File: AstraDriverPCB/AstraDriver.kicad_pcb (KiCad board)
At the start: 2 copper layers, 10 x 12 mm, 2 parts

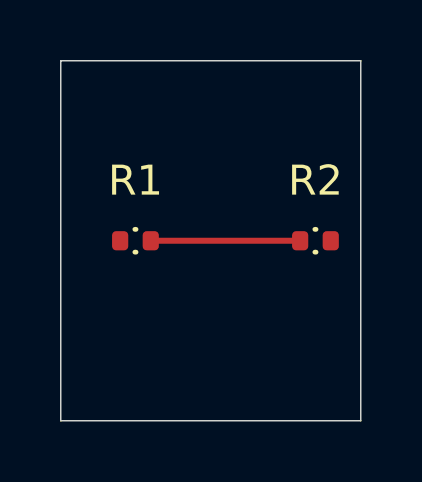
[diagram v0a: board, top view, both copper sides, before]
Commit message: Update board dimensions and center
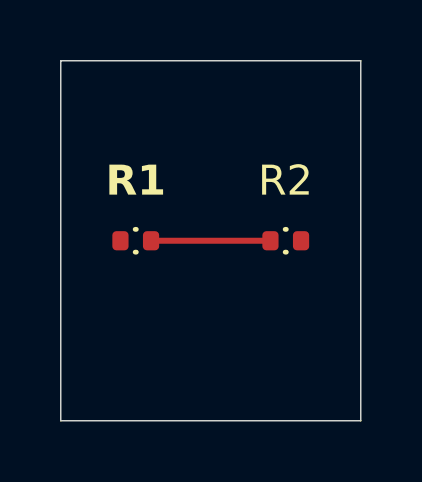
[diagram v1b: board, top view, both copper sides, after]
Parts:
- moved R2 0.99 mm to (147.5, 86.0)
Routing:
- net Net-(R1-Pad2): track 4.98 -> 3.98 mm
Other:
- copper layers 2 -> 4
- rule pad_to_mask_clearance: 0 -> 0.04
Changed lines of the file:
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@@
 	(generator_version "8.0")
 	(general
-		(thickness 1.6)
+		(thickness 1.6062)
 		(legacy_teardrops no)
 	)
 	(paper "A4")
 	(layers
-		(0 "F.Cu" signal)
-		(31 "B.Cu" signal)
+		(0 "F.Cu" mixed)
+		(1 "In1.Cu" power)
+		(2 "In2.Cu" power)
+		(31 "B.Cu" mixed)
 		(32 "B.Adhes" user "B.Adhesive")
 		(33 "F.Adhes" user "F.Adhesive")
@@
 		(49 "F.Fab" user)
 		(50 "User.1" user)
-		(51 "User.2" user)
+		(51 "User.2" user "Board.Alignment")
 		(52 "User.3" user)
 		(53 "User.4" user)
-		(54 "User.5" user)
+		(54 "User.5" user "Board.Center")
 		(55 "User.6" user)
 		(56 "User.7" user)
-		(57 "User.8" user)
-		(58 "User.9" user)
+		(57 "User.8" user "Board.Dimensions")
+		(58 "User.9" user "Board.Title")
 	)
 	(setup
-		(pad_to_mask_clearance 0)
+		(stackup
+			(layer "F.SilkS"
+				(type "Top Silk Screen")
+				(color "White")
+			)
+			(layer "F.Paste"
+				(type "Top Solder Paste")
+			)
+			(layer "F.Mask"
+				(type "Top Solder Mask")
+				(color "#0000002B")
+				(thickness 0.01)
+			)
+			(layer "F.Cu"
+				(type "copper")
+				(thickness 0.035)
+			)
+			(layer "dielectric 1"
+				(type "prepreg")
+				(color "FR4 natural")
+				(thickness 0.2104)
+				(material "FR4")
+				(epsilon_r 4.4)
+				(loss_tangent 0.02)
+			)
+			(layer "In1.Cu"
+				(type "copper")
+				(thickness 0.0152)
+			)
+			(layer "dielectric 2"
+				(type "core")
+				(color "FR4 natural")
+				(thickness 1.065)
+				(material "FR4")
+				(epsilon_r 4.6)
+				(loss_tangent 0.02)
+			)
+			(layer "In2.Cu"
+				(type "copper")
+				(thickness 0.0152)
+			)
+			(layer "dielectric 3"
+				(type "prepreg")
+				(color "FR4 natural")
+				(thickness 0.2104)
+				(material "FR4")
+				(epsilon_r 4.4)
+				(loss_tangent 0.02)
+			)
+			(layer "B.Cu"
+				(type "copper")
+				(thickness 0.035)
+			)
+			(layer "B.Mask"
+				(type "Bottom Solder Mask")
+				(color "#0000002B")
+				(thickness 0.01)
+			)
+			(layer "B.Paste"
+				(type "Bottom Solder Paste")
+			)
+			(layer "B.SilkS"
+				(type "Bottom Silk Screen")
+				(color "White")
+			)
+			(copper_finish "ENIG")
+			(dielectric_constraints yes)
+		)
+		(pad_to_mask_clearance 0.04)
+		(solder_mask_min_width 0.102)
 		(allow_soldermask_bridges_in_footprints no)
 		(pcbplotparams
@@
 	(footprint "LiveAstra:R_0402_1005Metric"
 		(layer "F.Cu")
-		(at 148.49 86)
+		(at 147.5 86)
 		(descr "Resistor SMD 0402 (1005 Metric), square (rectangular) end terminal, IPC_7351 nominal, (Body size source: IPC-SM-782 page 72, https://www.pcb-3d.com/wordpress/wp-content/uploads/ipc-sm-782a_amendment_1_and_2.pdf), generated with kicad-footprint-generator")
 		(tags "resistor")
 		(property "Reference" "R2"
-			(at 0 -2 0)
+			(at -0.01 -2 0)
 			(layer "F.SilkS")
 			(effects
 				(font
 					(size 1 1)
-					(thickness 0.15)
+					(thickness 0.2)
 				)
 			)
@@
 	(footprint "LiveAstra:R_0402_1005Metric"
 		(layer "F.Cu")
-		(at 142.49 86)
+		(at 142.5 86)
 		(descr "Resistor SMD 0402 (1005 Metric), square (rectangular) end terminal, IPC_7351 nominal, (Body size source: IPC-SM-782 page 72, https://www.pcb-3d.com/wordpress/wp-content/uploads/ipc-sm-782a_amendment_1_and_2.pdf), generated with kicad-footprint-generator")
 		(tags "resistor")
 		(property "Reference" "R1"
-			(at 0 -2 360)
+			(at 0 -2 0)
 			(layer "F.SilkS")
 			(effects
 				(font
 					(size 1 1)
-					(thickness 0.15)
+					(thickness 0.2)
+					(bold yes)
 				)
 			)
@@
 		(layer "Edge.Cuts")
 	)
+	(gr_rect
+		(start 139 80)
+		(end 151 92)
+		(stroke
+			(width 0.15)
+			(type default)
+		)
+		(fill none)
+		(layer "User.5")
+	)
+	(gr_rect
+		(start 139 80)
+		(end 151 92)
+		(stroke
+			(width 0.15)
+			(type default)
+		)
+		(fill none)
+		(layer "User.8")
+	)
 	(segment
-		(start 147.98 86)
-		(end 143 86)
+		(start 146.99 86)
+		(end 143.01 86)
 		(width 0.2)
 		(layer "F.Cu")

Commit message: Progress
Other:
- board text added: "${TITLE}"
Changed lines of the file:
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@@
 		)
 		(property "Value" "10"
-			(at 0 2 360)
+			(at 0 2 0)
 			(layer "F.Fab")
 			(effects
@@
 		)
 		(fp_text user "${REFERENCE}"
-			(at 0 1 360)
+			(at 0 1 0)
 			(layer "F.Fab")
 			(effects
@@
 		)
 		(fill none)
-		(layer "User.5")
+		(layer "User.2")
 	)
 	(gr_rect
@@
 		)
 		(fill none)
+		(layer "User.5")
+	)
+	(gr_rect
+		(start 139 80)
+		(end 151 92)
+		(stroke
+			(width 0.15)
+			(type default)
+		)
+		(fill none)
 		(layer "User.8")
 	)
+	(gr_text "${TITLE}"
+		(at 145 77.5 0)
+		(layer "User.9")
+		(effects
+			(font
+				(face "ING Me Headline")
+				(size 4 4)
+				(thickness 0.15)
+			)
+		)
+		(render_cache "" 0)
+	)
 	(segment

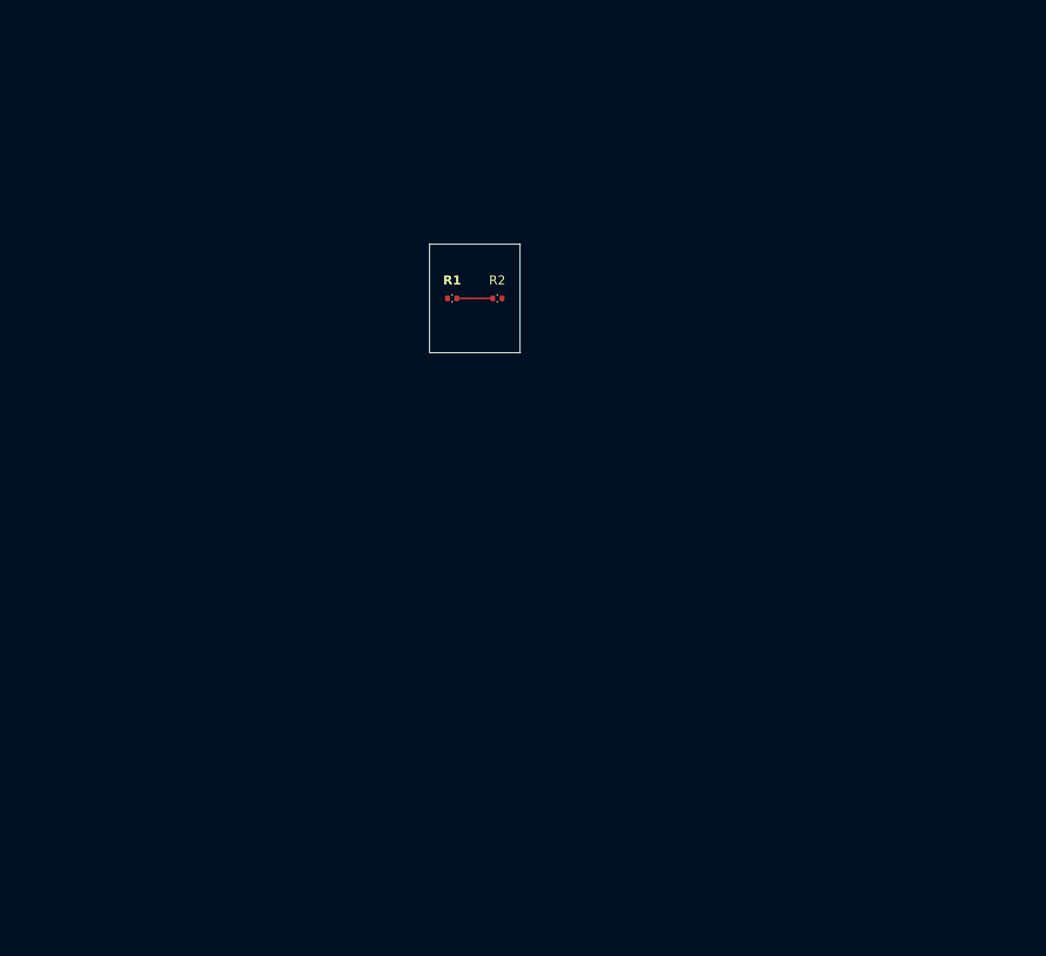
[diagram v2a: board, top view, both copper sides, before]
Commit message: Added all schematic components
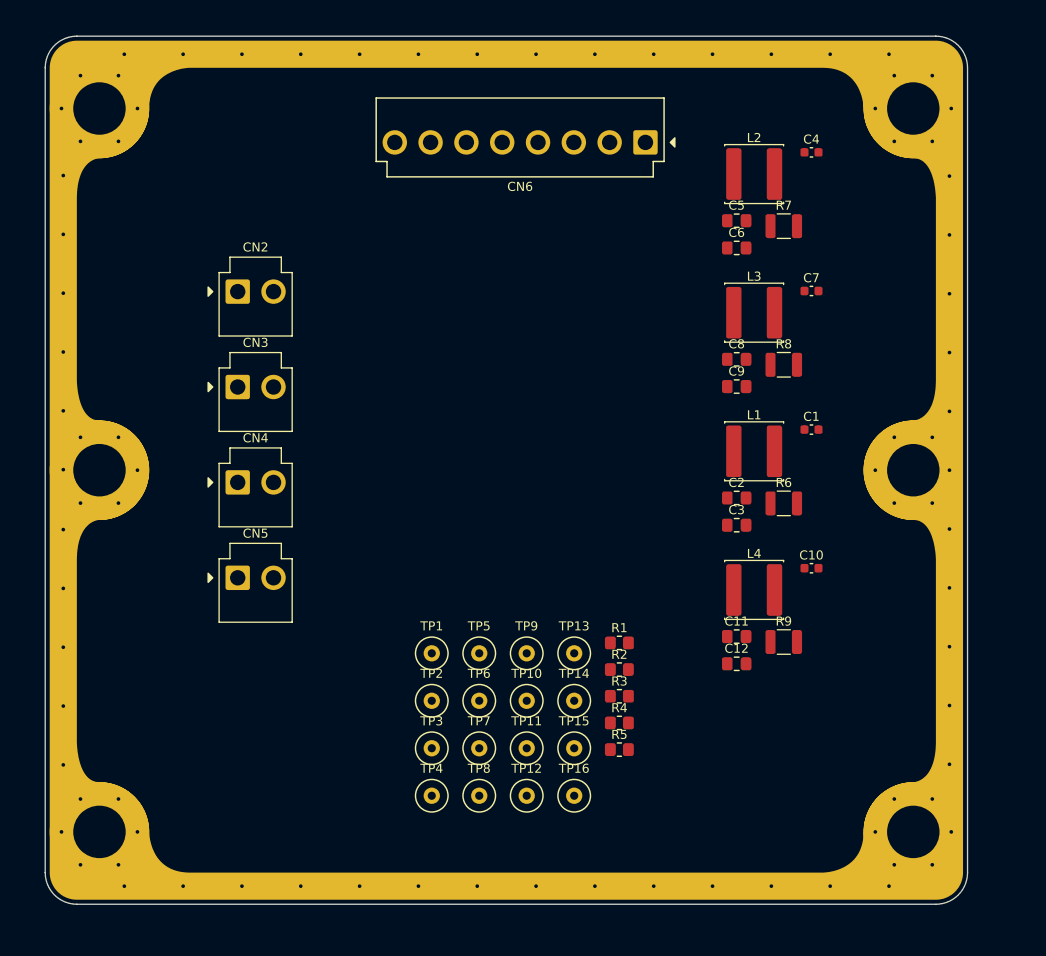
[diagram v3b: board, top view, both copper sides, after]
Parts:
- added C1: 22u, LiveAstra:C_0603_1608Metric, F.Cu at (182.2, 100.5)
- added C10: 22u, LiveAstra:C_0603_1608Metric, F.Cu at (182.2, 115.8)
- added C11: 1u, LiveAstra:C_0805_2012Metric_Pad1.18x1.45mm_HandSolder, F.Cu at (174.0, 123.4)
- added C12: 1u, LiveAstra:C_0805_2012Metric_Pad1.18x1.45mm_HandSolder, F.Cu at (174.0, 126.4)
- added C2: 1u, LiveAstra:C_0805_2012Metric_Pad1.18x1.45mm_HandSolder, F.Cu at (174.0, 108.1)
- added C3: 1u, LiveAstra:C_0805_2012Metric_Pad1.18x1.45mm_HandSolder, F.Cu at (174.0, 111.1)
- added C4: 22u, LiveAstra:C_0603_1608Metric, F.Cu at (182.2, 69.8)
- added C5: 1u, LiveAstra:C_0805_2012Metric_Pad1.18x1.45mm_HandSolder, F.Cu at (174.0, 77.4)
- added C6: 1u, LiveAstra:C_0805_2012Metric_Pad1.18x1.45mm_HandSolder, F.Cu at (174.0, 80.4)
- added C7: 22u, LiveAstra:C_0603_1608Metric, F.Cu at (182.2, 85.2)
- added C8: 1u, LiveAstra:C_0805_2012Metric_Pad1.18x1.45mm_HandSolder, F.Cu at (174.0, 92.7)
- added C9: 1u, LiveAstra:C_0805_2012Metric_Pad1.18x1.45mm_HandSolder, F.Cu at (174.0, 95.8)
- added CN2: JST VH 2 PIN, LiveAstra:JST_VH_B2P-VH-B_1x02_P3.96mm_Vertical, F.Cu at (120.8, 85.2)
- added CN3: JST VH 2 PIN, LiveAstra:JST_VH_B2P-VH-B_1x02_P3.96mm_Vertical, F.Cu at (120.8, 95.8)
- added CN4: JST VH 2 PIN, LiveAstra:JST_VH_B2P-VH-B_1x02_P3.96mm_Vertical, F.Cu at (120.8, 106.3)
- added CN5: JST VH 2 PIN, LiveAstra:JST_VH_B2P-VH-B_1x02_P3.96mm_Vertical, F.Cu at (120.8, 116.9)
- added CN6: JST VH 8 PIN, LiveAstra:JST_VH_B8P-VH-B_1x08_P3.96mm_Vertical, F.Cu at (150.0, 68.8)
- added L1: 4u7H, LiveAstra:L_Sunlord_SWPA6045S, F.Cu at (175.9, 102.9)
- added L2: 4u7H, LiveAstra:L_Sunlord_SWPA6045S, F.Cu at (175.9, 72.2)
- added L3: 4u7H, LiveAstra:L_Sunlord_SWPA6045S, F.Cu at (175.9, 87.6)
- added L4: 4u7H, LiveAstra:L_Sunlord_SWPA6045S, F.Cu at (175.9, 118.2)
- added R3: 0, LiveAstra:R_0805_2012Metric_Pad1.20x1.40mm_HandSolder, F.Cu at (161.0, 130.0)
- added R4: 0, LiveAstra:R_0805_2012Metric_Pad1.20x1.40mm_HandSolder, F.Cu at (161.0, 132.9)
- added R5: 0, LiveAstra:R_0805_2012Metric_Pad1.20x1.40mm_HandSolder, F.Cu at (161.0, 135.9)
- added R6: 40m, LiveAstra:R_1210_3225Metric, F.Cu at (179.2, 108.7)
- added R7: 40m, LiveAstra:R_1210_3225Metric, F.Cu at (179.2, 78.0)
- added R8: 40m, LiveAstra:R_1210_3225Metric, F.Cu at (179.2, 93.3)
- added R9: 47m, LiveAstra:R_1210_3225Metric, F.Cu at (179.2, 124.0)
- added RING1: ~, LiveAstra:AstraControl_Ground_Ring, F.Cu at (148.5, 105.0)
- added TP1: TestPoint_Thimble, LiveAstra:TestPoint_Loop_D3.50mm_Drill0.9mm_Beaded, F.Cu at (140.2, 125.2)
- added TP10: TestPoint_Thimble, LiveAstra:TestPoint_Loop_D3.50mm_Drill0.9mm_Beaded, F.Cu at (150.8, 130.5)
- added TP11: TestPoint_Thimble, LiveAstra:TestPoint_Loop_D3.50mm_Drill0.9mm_Beaded, F.Cu at (150.8, 135.8)
- added TP12: TestPoint_Thimble, LiveAstra:TestPoint_Loop_D3.50mm_Drill0.9mm_Beaded, F.Cu at (150.8, 141.0)
- added TP13: TestPoint_Thimble, LiveAstra:TestPoint_Loop_D3.50mm_Drill0.9mm_Beaded, F.Cu at (156.0, 125.2)
- added TP14: TestPoint_Thimble, LiveAstra:TestPoint_Loop_D3.50mm_Drill0.9mm_Beaded, F.Cu at (156.0, 130.5)
- added TP15: TestPoint_Thimble, LiveAstra:TestPoint_Loop_D3.50mm_Drill0.9mm_Beaded, F.Cu at (156.0, 135.8)
- added TP16: TestPoint_Thimble, LiveAstra:TestPoint_Loop_D3.50mm_Drill0.9mm_Beaded, F.Cu at (156.0, 141.0)
- added TP2: TestPoint_Thimble, LiveAstra:TestPoint_Loop_D3.50mm_Drill0.9mm_Beaded, F.Cu at (140.2, 130.5)
- added TP3: TestPoint_Thimble, LiveAstra:TestPoint_Loop_D3.50mm_Drill0.9mm_Beaded, F.Cu at (140.2, 135.8)
- added TP4: TestPoint_Thimble, LiveAstra:TestPoint_Loop_D3.50mm_Drill0.9mm_Beaded, F.Cu at (140.2, 141.0)
- added TP5: TestPoint_Thimble, LiveAstra:TestPoint_Loop_D3.50mm_Drill0.9mm_Beaded, F.Cu at (145.5, 125.2)
- added TP6: TestPoint_Thimble, LiveAstra:TestPoint_Loop_D3.50mm_Drill0.9mm_Beaded, F.Cu at (145.5, 130.5)
- added TP7: TestPoint_Thimble, LiveAstra:TestPoint_Loop_D3.50mm_Drill0.9mm_Beaded, F.Cu at (145.5, 135.8)
- added TP8: TestPoint_Thimble, LiveAstra:TestPoint_Loop_D3.50mm_Drill0.9mm_Beaded, F.Cu at (145.5, 141.0)
- added TP9: TestPoint_Thimble, LiveAstra:TestPoint_Loop_D3.50mm_Drill0.9mm_Beaded, F.Cu at (150.8, 125.2)
- R1, R2: value 10 -> 0; footprint LiveAstra:R_0402_1005Metric -> LiveAstra:R_0805_2012Metric_Pad1.20x1.40mm_HandSolder
- moved R2 43.2 mm to (161.0, 127.0)
- moved R1 42.4 mm to (161.0, 124.1)
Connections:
- R1 pad 1: GND -> /Block Diagram/PWM_CH4
- R1 pad 2: Net-(R1-Pad2) -> /Block Diagram/Channel 4 2A/DIM
- R2 pad 1: Net-(R1-Pad2) -> /Block Diagram/PWM_CH3
- R2 pad 2: unconnected-(R2-Pad2) -> /Block Diagram/Channel 3 2.5A/DIM
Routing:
- net Net-(R1-Pad2): track 3.98 -> 0.00 mm
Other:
- board size 10 x 12 mm -> 102 x 96 mm

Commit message: progress
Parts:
- removed C10: 22u, LiveAstra:C_0603_1608Metric
- removed C11, C12: 1u, LiveAstra:C_0805_2012Metric_Pad1.18x1.45mm_HandSolder
- added C13: 1u, LiveAstra:C_0805_2012Metric_Pad1.18x1.45mm_HandSolder, F.Cu at (178.8, 101.2)
- added C14: 1u, LiveAstra:C_0805_2012Metric_Pad1.18x1.45mm_HandSolder, F.Cu at (157.7, 114.2)
- added C15: 1u, LiveAstra:C_0805_2012Metric_Pad1.18x1.45mm_HandSolder, F.Cu at (141.2, 115.5)
- added U1: LED2001PHR, LiveAstra:U_LED2001PHR_HSOP8, F.Cu at (177.5, 108.6)
- added U2: LED2001PHR, LiveAstra:U_LED2001PHR_HSOP8, F.Cu at (157.3, 101.6)
- added U3: LED2001PHR, LiveAstra:U_LED2001PHR_HSOP8, F.Cu at (140.7, 106.7)
- added U4: LED2001PHR, LiveAstra:U_LED2001PHR_HSOP8, F.Cu at (117.8, 116.6)
- C1, C4, C7: footprint LiveAstra:C_0603_1608Metric -> LiveAstra:C_0805_2012Metric_Pad1.18x1.45mm_HandSolder
- C9: value 1u -> 22u
- moved C6 71.9 mm to (114.8, 121.3)
- moved C8 67.0 mm to (114.8, 124.3)
- moved CN5 59.9 mm to (175.5, 141.2), turned to 180 degrees
- moved TP8 58.5 mm to (162.2, 85.0)
- moved TP4 57.3 mm to (142.8, 83.8)
- moved R5 56.9 mm to (162.2, 79.0), turned to -90 degrees
- moved CN2 56.0 mm to (121.5, 141.2), turned to 180 degrees
- moved L4 54.5 mm to (121.8, 124.0)
- moved R4 54.0 mm to (157.8, 79.0), turned to -90 degrees
- moved R9 53.7 mm to (125.7, 118.5)
- moved C7 53.4 mm to (137.0, 113.5)
- moved C9 53.3 mm to (124.5, 115.5)
- moved TP7 52.9 mm to (157.8, 84.2)
- moved TP3 52.3 mm to (137.2, 83.5)
- moved R3 51.9 mm to (153.0, 78.8), turned to -90 degrees
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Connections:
- net /Block Diagram/Channel 1 2.5A/DIM renamed /Block Diagram/DIM_1
- net /Block Diagram/Channel 1 2.5A/LED- renamed /Block Diagram/CH1_LED-
- net /Block Diagram/Channel 2 2.5A/DIM renamed /Block Diagram/DIM_2
- net /Block Diagram/Channel 3 2.5A/DIM renamed /Block Diagram/DIM_3
- net /Block Diagram/Channel 4 2A/DIM renamed /Block Diagram/DIM_4
- net Net-(R5-Pad2) renamed /Block Diagram/RSRV
- C3 pad 2: /Block Diagram/Channel 1 2.5A/LED+ -> +5V
- C6 pad 2: /Block Diagram/Channel 2 2.5A/LED+ -> /Block Diagram/CH4_LED+
- C9 pad 2: /Block Diagram/Channel 3 2.5A/LED+ -> +5V
- CN2 pad 1: /Block Diagram/Channel 4 2A/LED+ -> /Block Diagram/CH4_LED+
- CN2 pad 2: /Block Diagram/Channel 4 2A/LED- -> /Block Diagram/CH4_LED+
- CN3 pad 1: /Block Diagram/Channel 3 2.5A/LED+ -> /Block Diagram/CH3_LED+
- CN3 pad 2: /Block Diagram/Channel 3 2.5A/LED- -> /Block Diagram/CH3_LED+
- CN4 pad 1: /Block Diagram/Channel 2 2.5A/LED+ -> /Block Diagram/CH2_LED+
- CN4 pad 2: /Block Diagram/Channel 2 2.5A/LED- -> /Block Diagram/CH2_LED+
- CN5 pad 1: /Block Diagram/Channel 1 2.5A/LED+ -> /Block Diagram/CH1_LED+
- CN6 pad 1: /Block Diagram/RESERVED -> +5V
- CN6 pad 2: /Block Diagram/PWM_CH1 -> +3V3
- CN6 pad 3: /Block Diagram/PWM_CH2 -> GND
- CN6 pad 4: /Block Diagram/PWM_CH3 -> /Block Diagram/PWM_CH4
- CN6 pad 5: /Block Diagram/PWM_CH4 -> /Block Diagram/PWM_CH3
- CN6 pad 6: GND -> /Block Diagram/PWM_CH2
- CN6 pad 7: +3V3 -> /Block Diagram/PWM_CH1
- CN6 pad 8: +5V -> /Block Diagram/RESERVED
- L1 pad 1: Net-(U1-SW) -> /Block Diagram/Channel 1 2.5A/SW_OUT
- L1 pad 2: /Block Diagram/Channel 1 2.5A/LED+ -> /Block Diagram/CH1_LED+
- L2 pad 1: Net-(U2-SW) -> /Block Diagram/Channel 2 2.5A/SW_OUT
- L2 pad 2: /Block Diagram/Channel 2 2.5A/LED+ -> /Block Diagram/CH2_LED+
- L3 pad 1: Net-(U3-SW) -> /Block Diagram/Channel 3 2.5A/SW_OUT
- L3 pad 2: /Block Diagram/Channel 3 2.5A/LED+ -> /Block Diagram/CH3_LED+
- L4 pad 1: Net-(U4-SW) -> /Block Diagram/Channel 4 2A/SW_OUT
- L4 pad 2: /Block Diagram/Channel 4 2A/LED+ -> /Block Diagram/CH4_LED+
- R7 pad 2: /Block Diagram/Channel 2 2.5A/LED- -> /Block Diagram/CH2_LED+
- R8 pad 2: /Block Diagram/Channel 3 2.5A/LED- -> /Block Diagram/CH3_LED+
- R9 pad 2: /Block Diagram/Channel 4 2A/LED- -> /Block Diagram/CH4_LED+
- TP10 pad 1: /Block Diagram/Channel 4 2A/LED- -> /Block Diagram/CH4_LED+
- TP11 pad 1: /Block Diagram/Channel 3 2.5A/LED+ -> /Block Diagram/CH3_LED+
- TP12 pad 1: /Block Diagram/Channel 3 2.5A/LED- -> /Block Diagram/CH3_LED+
- TP13 pad 1: /Block Diagram/Channel 2 2.5A/LED+ -> /Block Diagram/CH2_LED+
- TP14 pad 1: /Block Diagram/Channel 2 2.5A/LED- -> /Block Diagram/CH2_LED+
- TP15 pad 1: /Block Diagram/Channel 1 2.5A/LED+ -> /Block Diagram/CH1_LED+
- TP9 pad 1: /Block Diagram/Channel 4 2A/LED+ -> /Block Diagram/CH4_LED+
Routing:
- net GND: vias 0 -> 4
- net /Block Diagram/Channel 1 2.5A/SW_OUT: vias 0 -> 5
- added copper zone on F.Cu, net /Block Diagram/Channel 1 2.5A/SW_OUT

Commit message: Finished layout
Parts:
- added R10: 0, LiveAstra:R_0805_2012Metric_Pad1.20x1.40mm_HandSolder, F.Cu at (133.2, 78.8)
- moved L4 22.8 mm to (115.7, 102.0), turned to 180 degrees
- moved L3 18.9 mm to (133.7, 102.0), turned to 180 degrees
- moved C3 18.0 mm to (157.4, 113.2)
- moved C6 14.4 mm to (116.2, 107.0), turned to 180 degrees
- moved L1 14.1 mm to (169.7, 102.0), turned to 180 degrees
- moved C9 13.5 mm to (123.8, 102.0)
- moved TP8 13.3 mm to (175.5, 85.5)
- moved R8 12.9 mm to (144.5, 114.0), turned to 180 degrees
- moved C8 12.9 mm to (121.4, 113.2)
- moved C7 12.4 mm to (141.8, 102.0)
- moved C15 11.0 mm to (134.2, 107.0), turned to 180 degrees
- moved U4 10.5 mm to (124.4, 108.5), turned to 90 degrees
- moved C13 10.3 mm to (170.2, 107.0), turned to 180 degrees
- moved TP7 10.1 mm to (167.8, 85.5)
- moved L2 9.42 mm to (151.7, 102.0), turned to 180 degrees
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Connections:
- CN2 pad 1: /Block Diagram/CH4_LED+ -> /Block Diagram/CH4_LED-
- CN3 pad 1: /Block Diagram/CH3_LED+ -> /Block Diagram/CH3_LED-
- CN4 pad 1: /Block Diagram/CH2_LED+ -> /Block Diagram/CH2_LED-
- CN5 pad 1: /Block Diagram/CH1_LED+ -> /Block Diagram/CH1_LED-
- CN5 pad 2: /Block Diagram/CH1_LED- -> /Block Diagram/CH1_LED+
- CN6 pad 2: +3V3 -> /Block Diagram/3V3_R
- R7 pad 2: /Block Diagram/CH2_LED+ -> /Block Diagram/CH2_LED-
- R8 pad 2: /Block Diagram/CH3_LED+ -> /Block Diagram/CH3_LED-
- R9 pad 2: /Block Diagram/CH4_LED+ -> /Block Diagram/CH4_LED-
- TP11 pad 1: /Block Diagram/CH3_LED+ -> /Block Diagram/CH3_LED-
- TP13 pad 1: /Block Diagram/CH2_LED+ -> /Block Diagram/CH2_LED-
- TP15 pad 1: /Block Diagram/CH1_LED+ -> /Block Diagram/CH1_LED-
- TP16 pad 1: /Block Diagram/CH1_LED- -> /Block Diagram/CH1_LED+
- TP9 pad 1: /Block Diagram/CH4_LED+ -> /Block Diagram/CH4_LED-
- U2 pad 3: /Block Diagram/CH2_LED+ -> /Block Diagram/CH2_LED-
- U3 pad 3: /Block Diagram/CH3_LED+ -> /Block Diagram/CH3_LED-
- U4 pad 3: /Block Diagram/CH4_LED+ -> /Block Diagram/CH4_LED-
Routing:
- net /Block Diagram/DIM_1: track 0.00 -> 52.7 mm, vias 0 -> 2
- net /Block Diagram/DIM_4: track 0.00 -> 50.6 mm, vias 0 -> 2
- net /Block Diagram/DIM_2: track 0.00 -> 43.7 mm, vias 0 -> 2
- net /Block Diagram/DIM_3: track 0.00 -> 43.5 mm, vias 0 -> 2
- net +5V: track 0.00 -> 18.0 mm, vias 0 -> 56
- net /Block Diagram/RSRV: track 0.00 -> 14.1 mm
- net /Block Diagram/PWM_CH4: track 0.00 -> 12.0 mm
- net /Block Diagram/3V3_R: track 0.00 -> 11.2 mm
- net /Block Diagram/PWM_CH3: track 0.00 -> 11.1 mm
- net /Block Diagram/PWM_CH2: track 0.00 -> 10.2 mm
- net /Block Diagram/RESERVED: track 0.00 -> 9.58 mm
- net /Block Diagram/PWM_CH1: track 0.00 -> 9.31 mm
- net +3V3: track 0.00 -> 7.42 mm
- net /Block Diagram/CH4_LED-: track 0.00 -> 3.03 mm
- net /Block Diagram/CH3_LED-: track 0.00 -> 3.03 mm
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- added copper zone on F.Cu, net +5V
- added copper zone on In2.Cu, net +5V
- added copper zone on F.Cu, net /Block Diagram/CH1_LED+
- added copper zone on F.Cu, net /Block Diagram/CH1_LED-
- added copper zone on F.Cu, net /Block Diagram/CH2_LED+
- added copper zone on F.Cu, net /Block Diagram/CH2_LED-
- added copper zone on F.Cu, net /Block Diagram/CH3_LED+
- added copper zone on F.Cu, net /Block Diagram/CH3_LED-
- added copper zone on F.Cu, net /Block Diagram/CH4_LED+
- added copper zone on F.Cu, net /Block Diagram/CH4_LED-
- added copper zone on B.Cu, net /Block Diagram/Channel 1 2.5A/SW_OUT
- added copper zone on B.Cu, net /Block Diagram/Channel 2 2.5A/SW_OUT
- added copper zone on F.Cu, net /Block Diagram/Channel 2 2.5A/SW_OUT
- added copper zone on B.Cu, net /Block Diagram/Channel 3 2.5A/SW_OUT
- added copper zone on F.Cu, net /Block Diagram/Channel 3 2.5A/SW_OUT
- added copper zone on B.Cu, net /Block Diagram/Channel 4 2A/SW_OUT
- added copper zone on F.Cu, net /Block Diagram/Channel 4 2A/SW_OUT
- added copper zone on B.Cu, net GND
- added copper zone on F.Cu, net GND
- added copper zone on In1.Cu, net GND
